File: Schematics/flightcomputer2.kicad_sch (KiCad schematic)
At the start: 0 parts

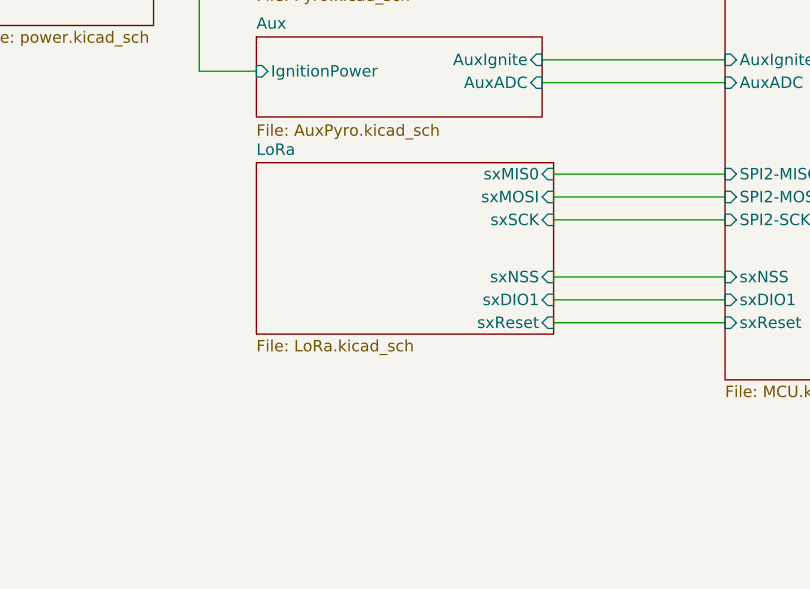
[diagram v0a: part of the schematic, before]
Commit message: added DIO0 and DIO2 pins to read lora module outputs
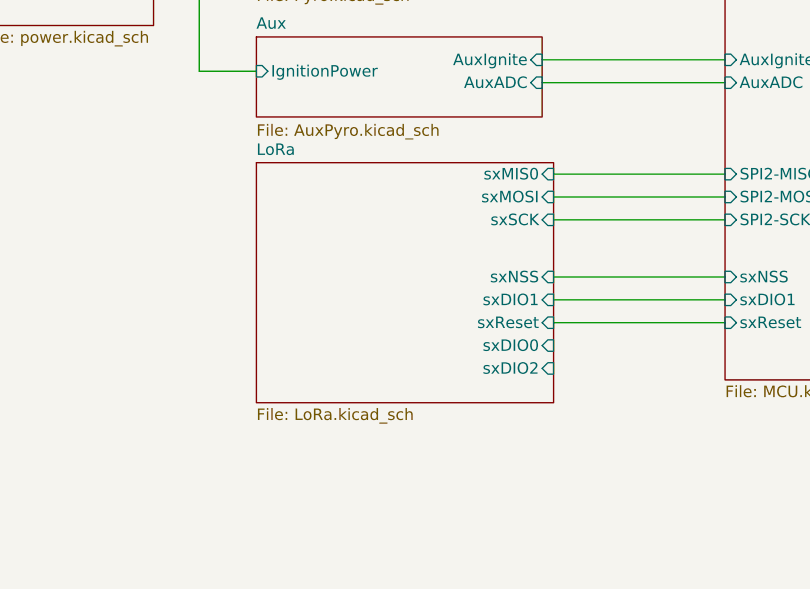
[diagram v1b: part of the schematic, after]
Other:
- sheet LoRa ports: added sxDIO0, sxDIO2; removed none
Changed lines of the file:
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@@
 	(sheet
 		(at 59.69 124.46)
-		(size 33.02 19.05)
+		(size 33.02 26.67)
 		(exclude_from_sim no)
 		(in_bom yes)
@@
 		)
 		(property "Sheetfile" "LoRa.kicad_sch"
-			(at 59.69 144.0946 0)
+			(at 59.69 151.7146 0)
 			(effects
 				(font
@@
 			(effects
 				(font
+					(size 1.27 1.27)
+				)
+				(justify right)
+			)
+		)
+		(pin "sxDIO0" input
+			(at 92.71 144.78 0)
+			(effects
+				(font
+					(size 1.27 1.27)
+				)
+				(justify right)
+			)
+		)
+		(pin "sxDIO2" input
+			(at 92.71 147.32 0)
+			(effects
+				(font
